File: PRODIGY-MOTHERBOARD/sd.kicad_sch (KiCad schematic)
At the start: 11 parts, among them J21 DM3BT-DSF-PEJS/C, U27 IP4252CZ16, U28 RT9742AGJ5F

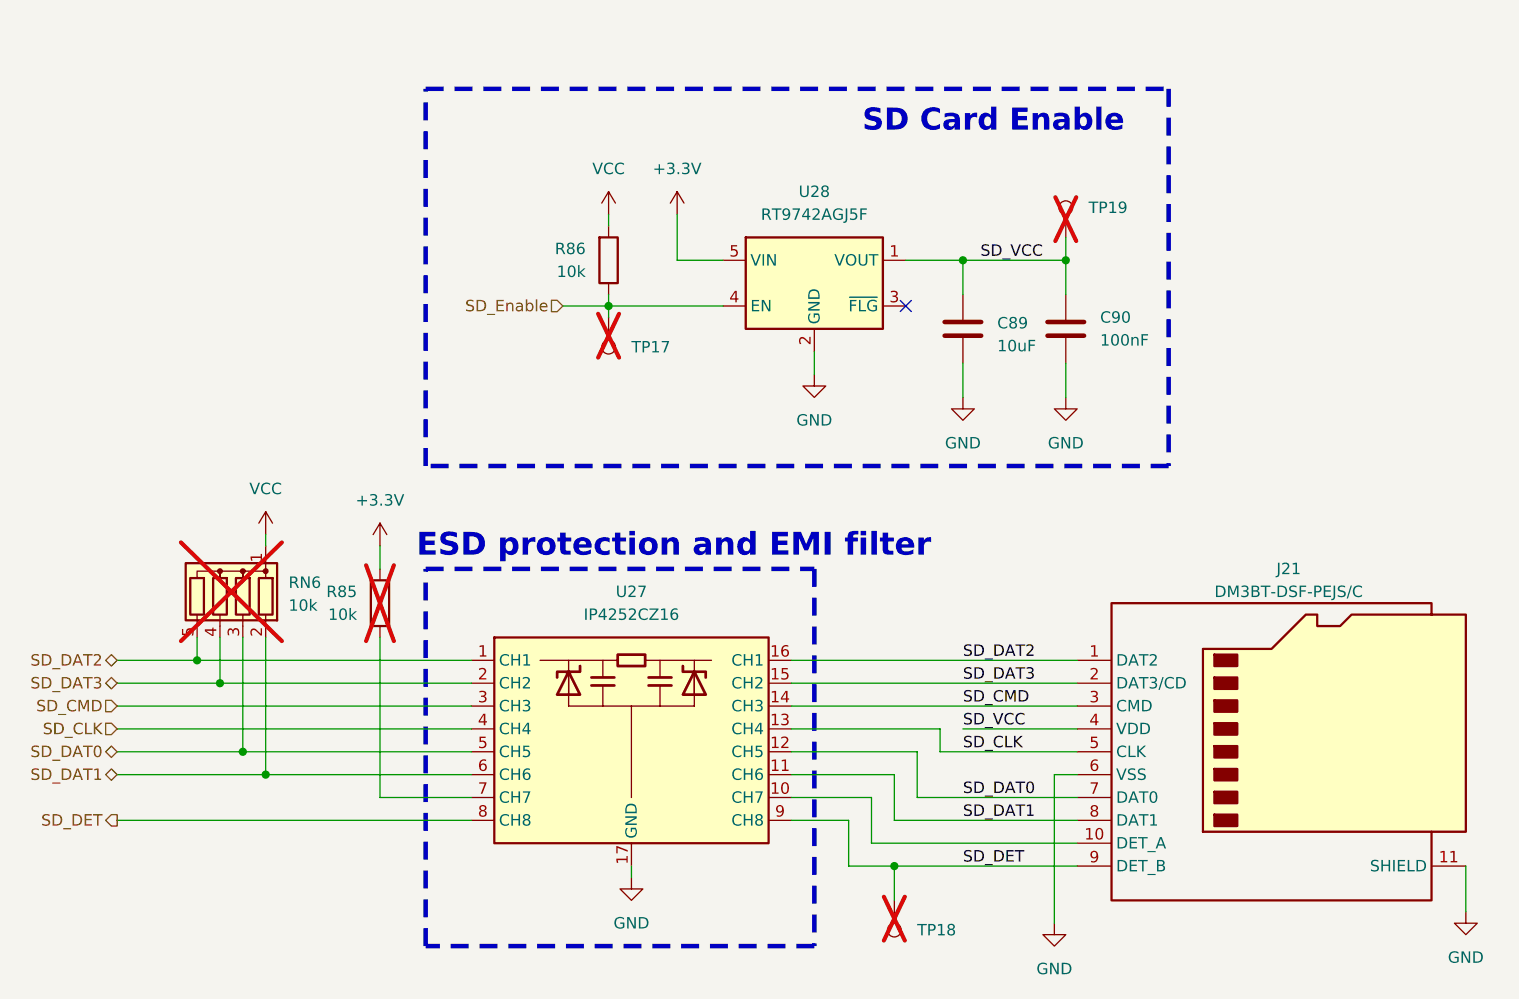
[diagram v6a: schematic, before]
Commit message: Resistor array fixed, layout main components locked, high speed routing done
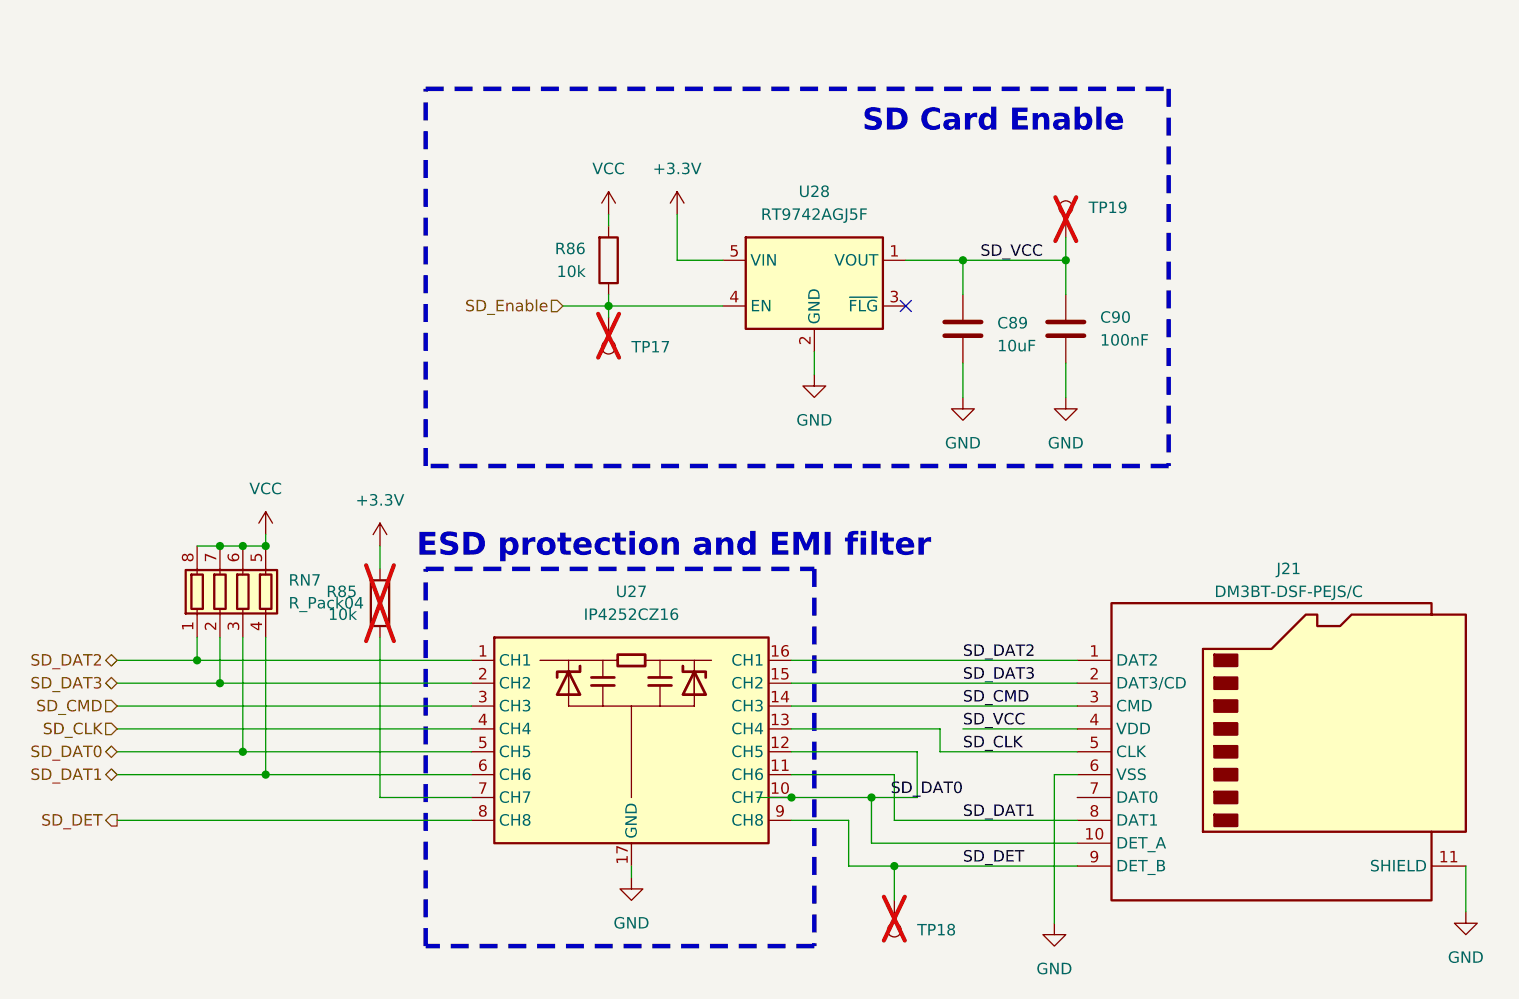
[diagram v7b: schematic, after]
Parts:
- removed RN6: 10k, Resistor_SMD:R_Array_Convex_4x0603, symbol Device:R_Network04
- added RN7: R_Pack04, Resistor_SMD:R_Array_Convex_4x0603, symbol Device:R_Pack04
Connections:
- net SD_DAT0: now also RN7.3 (R3.1); no longer J21.7 (DAT0), U27.12 (CH5)
- net SD_DAT1: now also RN7.4 (R4.1)
- net SD_DAT2: now also RN7.1 (R1.1)
- net SD_DAT3: now also RN7.2 (R2.1)
- net VCC: now also RN7.5 (R4.2), RN7.6 (R3.2), RN7.7 (R2.2), RN7.8 (R1.2)
- net at J21.10 (DET_A), U27.10 (CH7): now also U27.12 (CH5)

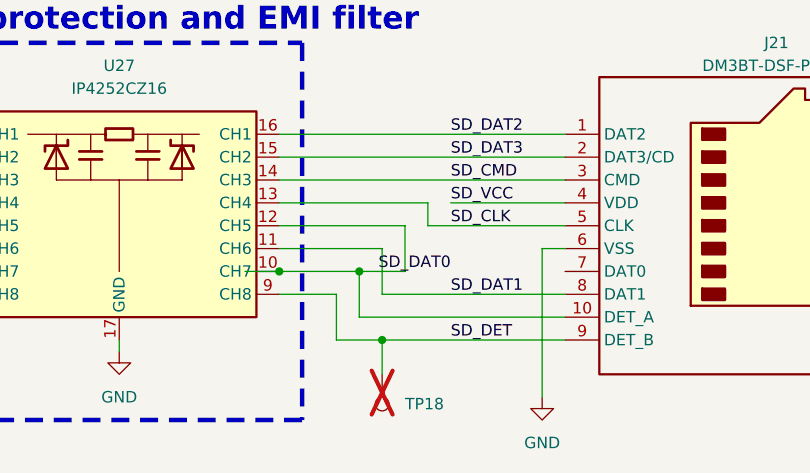
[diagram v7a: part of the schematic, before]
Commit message: motherboard bulk routing mostly done, loads of vias placed, should be done with one days work
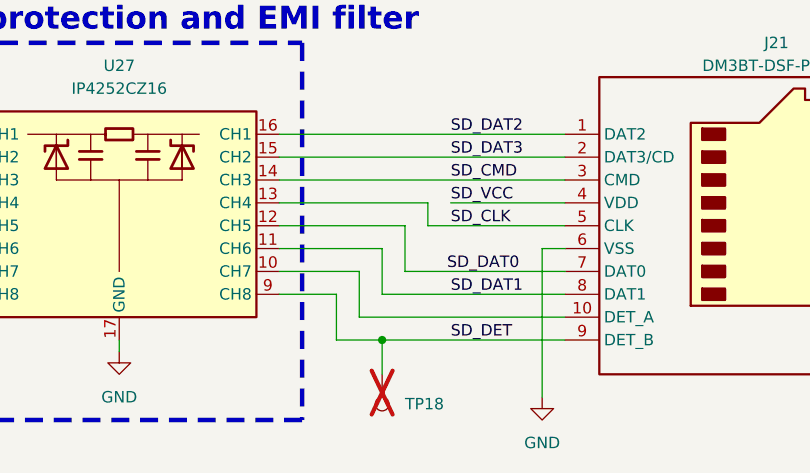
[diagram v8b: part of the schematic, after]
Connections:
- net SD_DAT0: now also J21.7 (DAT0), U27.12 (CH5)
- net at J21.10 (DET_A), U27.10 (CH7): no longer U27.12 (CH5)
